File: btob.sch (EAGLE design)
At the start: 4 parts, among them J1 MLE-105-01-G-DV, J2 MLE-105-01-G-DV, J3 MLE-105-01-G-DV

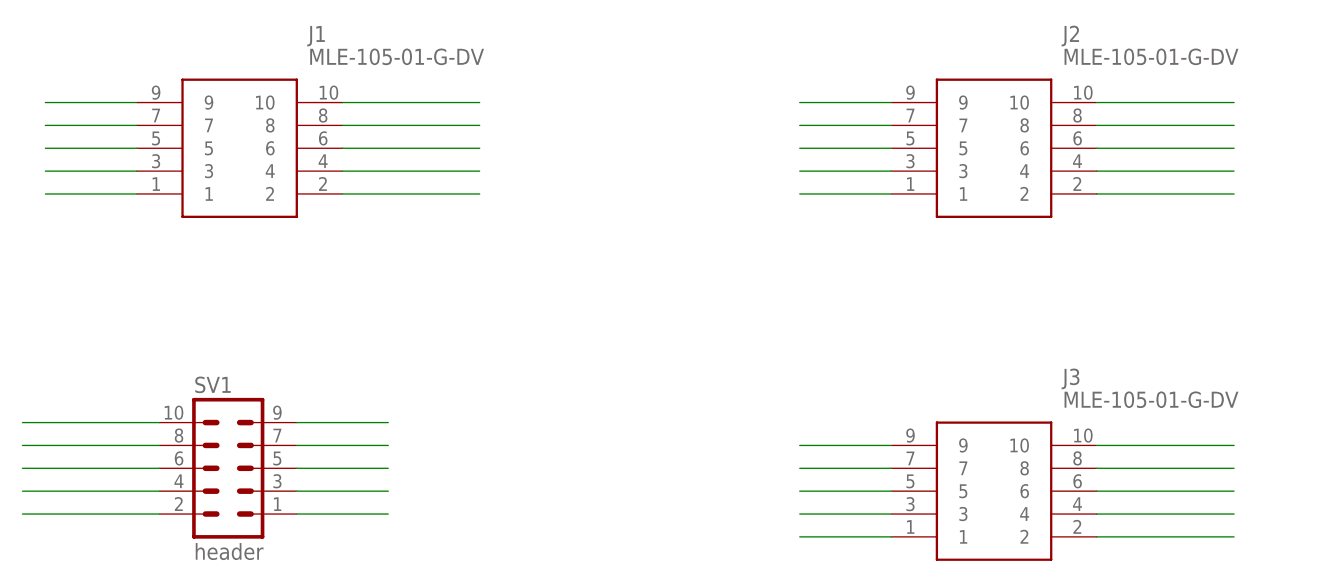
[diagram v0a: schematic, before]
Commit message: rework for small sensor board with SCL imu chip
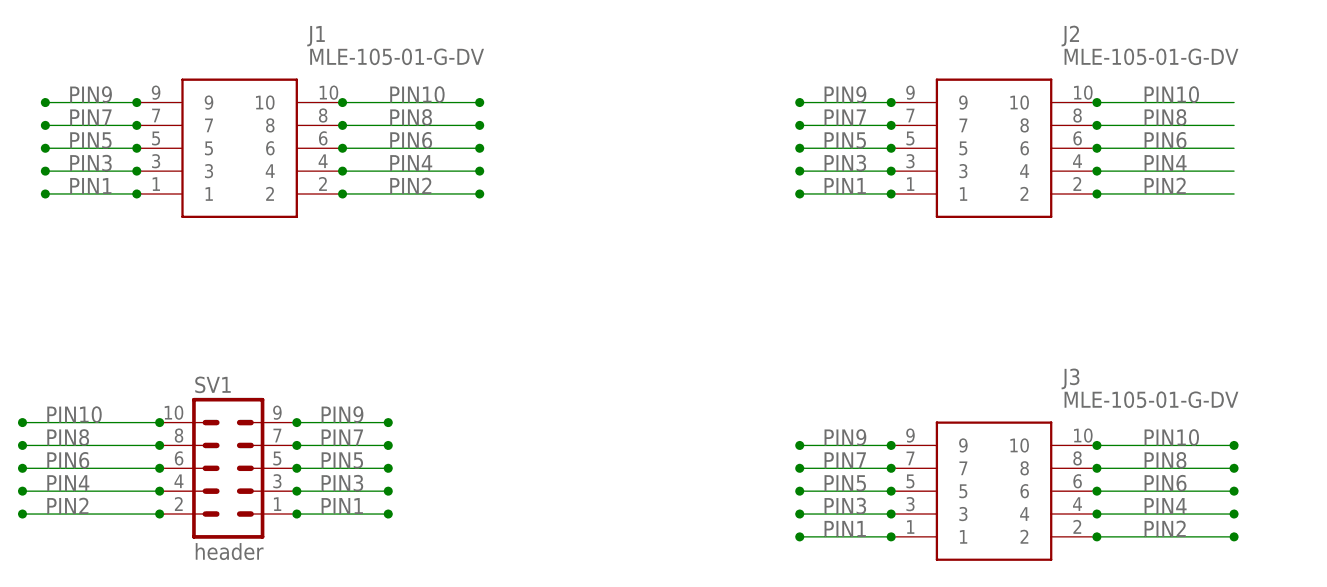
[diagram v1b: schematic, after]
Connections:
- net N$1 renamed PIN9
- net N$10 renamed PIN2
- net N$2 renamed PIN7
- net N$3 renamed PIN5
- net N$4 renamed PIN3
- net N$5 renamed PIN1
- net N$6 renamed PIN10
- net N$7 renamed PIN8
- net N$8 renamed PIN6
- net N$9 renamed PIN4
